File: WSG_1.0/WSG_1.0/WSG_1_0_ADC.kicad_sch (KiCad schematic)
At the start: 57 parts, among them J1 Conn_01x10, U1 ADS131A04IPBSR, U14 TPD4E1U06DBVR, U2 DAC60501ZDGSR, U3 INA827AIDGKR, U4 INA827AIDGKR, U5 INA827AIDGKR, U6 TMP235A2DBZR, Y1 SiT8008AI-13-33S-16.384000

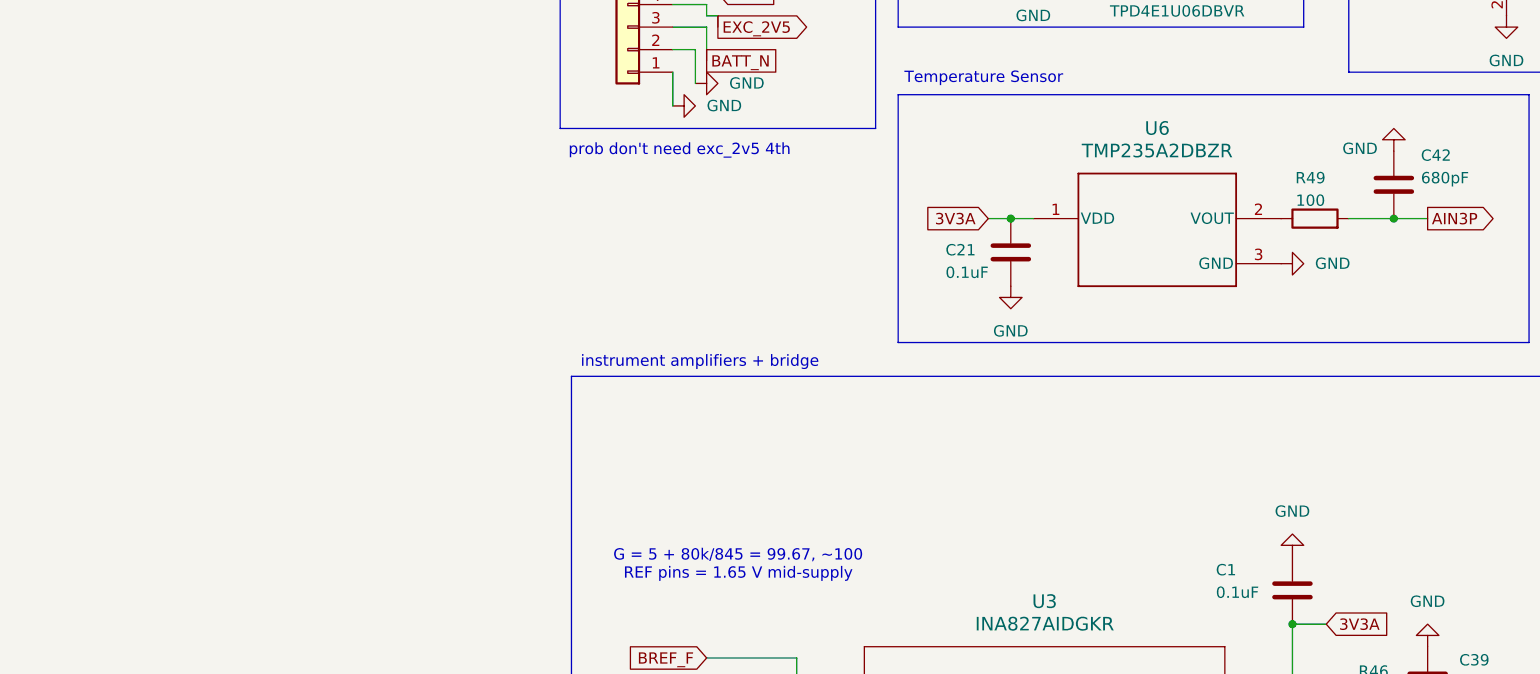
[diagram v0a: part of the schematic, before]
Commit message: labeled schematic flags, now doing routing stuff
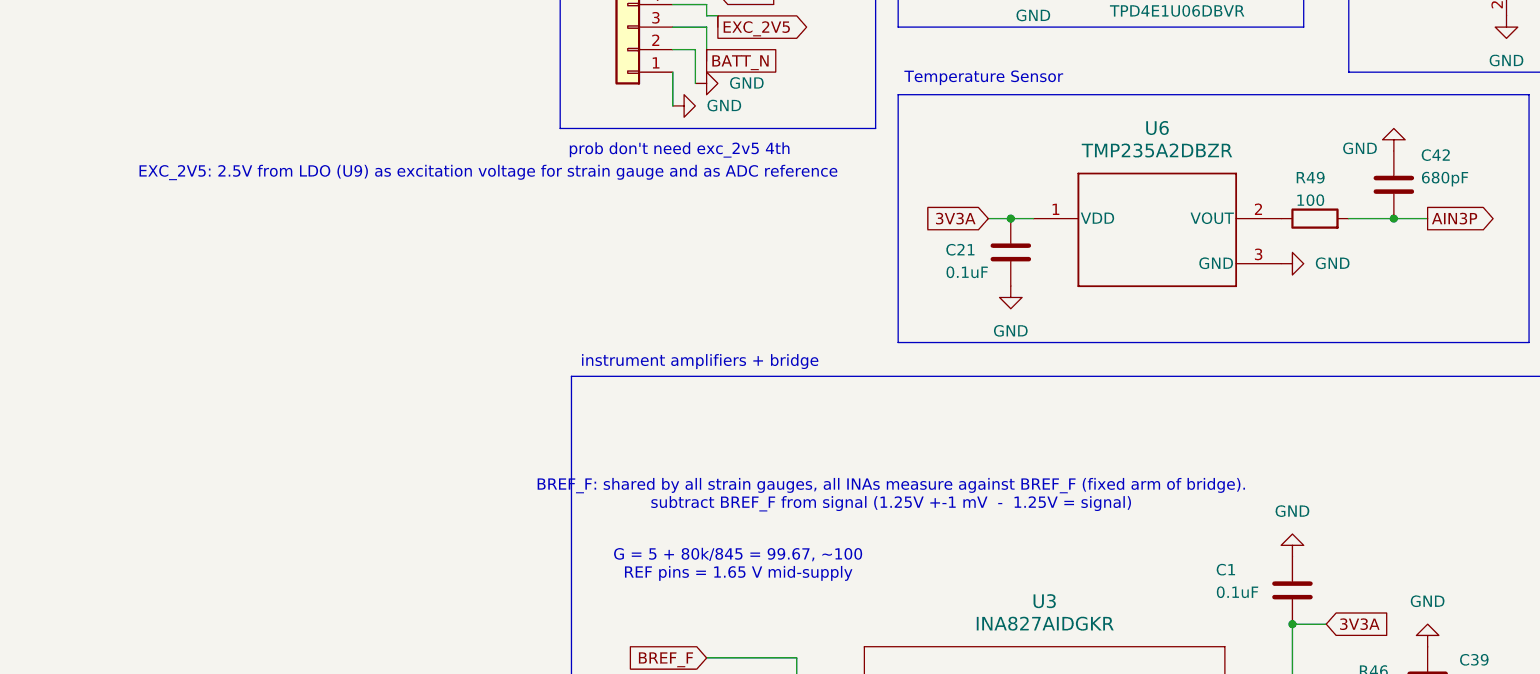
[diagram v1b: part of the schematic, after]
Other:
- note added: "BREF_F: shared by all strain gauges, all INAs measure against BREF_F (fixed arm of bridge). subtract BREF_F from signal (1.25V +-1 mV - 1.25V = signal)"
- note added: "EXC_2V5: 2.5V from LDO (U9) as excitation voltage for strain gauge and as ADC reference"
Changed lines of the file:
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@@
+		)
+	)
+	(text "BREF_F: shared by all strain gauges, all INAs measure against BREF_F (fixed arm of bridge). \nsubtract BREF_F from signal (1.25V +-1 mV  -  1.25V = signal)"
+		(exclude_from_sim no)
+		(at 50.038 94.742 0)
+		(effects
+			(font
+				(size 1.27 1.27)
+			)
 		)
 	)
@@
 		(effects
 			(font
+				(size 1.27 1.27)
+			)
+		)
+	)
+	(text "EXC_2V5: 2.5V from LDO (U9) as excitation voltage for strain gauge and as ADC reference"
+		(exclude_from_sim no)
+		(at 4.572 58.42 0)
+		(effects
+			(font

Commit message: schematic changes finished?
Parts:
- C39, C40, C41: value 2.7nF -> 150nF
- C42: value 680pF -> 150nF
- R46, R47, R48, R49, R50, R51, R52, R53: value 100 -> 1k
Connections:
- net GND: no longer C39.2, C40.2, C41.2, C42.2
- net AIN3N: now reaches R53.2, U1.7 (AIN4N)
- net AIN3N: now also C42.2
- net AIN0N: now reaches R51.2, U1.1 (AIN1N)
- net AIN0N: now also C39.2
- net AIN1N: now reaches R50.2, U1.3 (AIN2N)
- net AIN1N: now also C40.2
- net AIN2N: now reaches R52.2, U1.5 (AIN3N)
- net AIN2N: now also C41.2
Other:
- note added: "batt_n will be shorted to GND through the connector"
- note removed: "prob don't need exc_2v5 4th"
- moved on the sheet: R50, R52, R53

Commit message: production files generated
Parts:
- Y1: value SiT8008AI-13-33S-16.384000 -> DSC1001DI1-016.3840
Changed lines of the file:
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@@
 			)
 		)
-		(property "Value" "SiT8008AI-13-33S-16.384000"
+		(property "Value" "DSC1001DI1-016.3840"
 			(at 140.208 43.688 0)
 			(show_name no)
